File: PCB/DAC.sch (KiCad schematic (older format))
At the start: 3 parts, among them U9 DAC084S085C

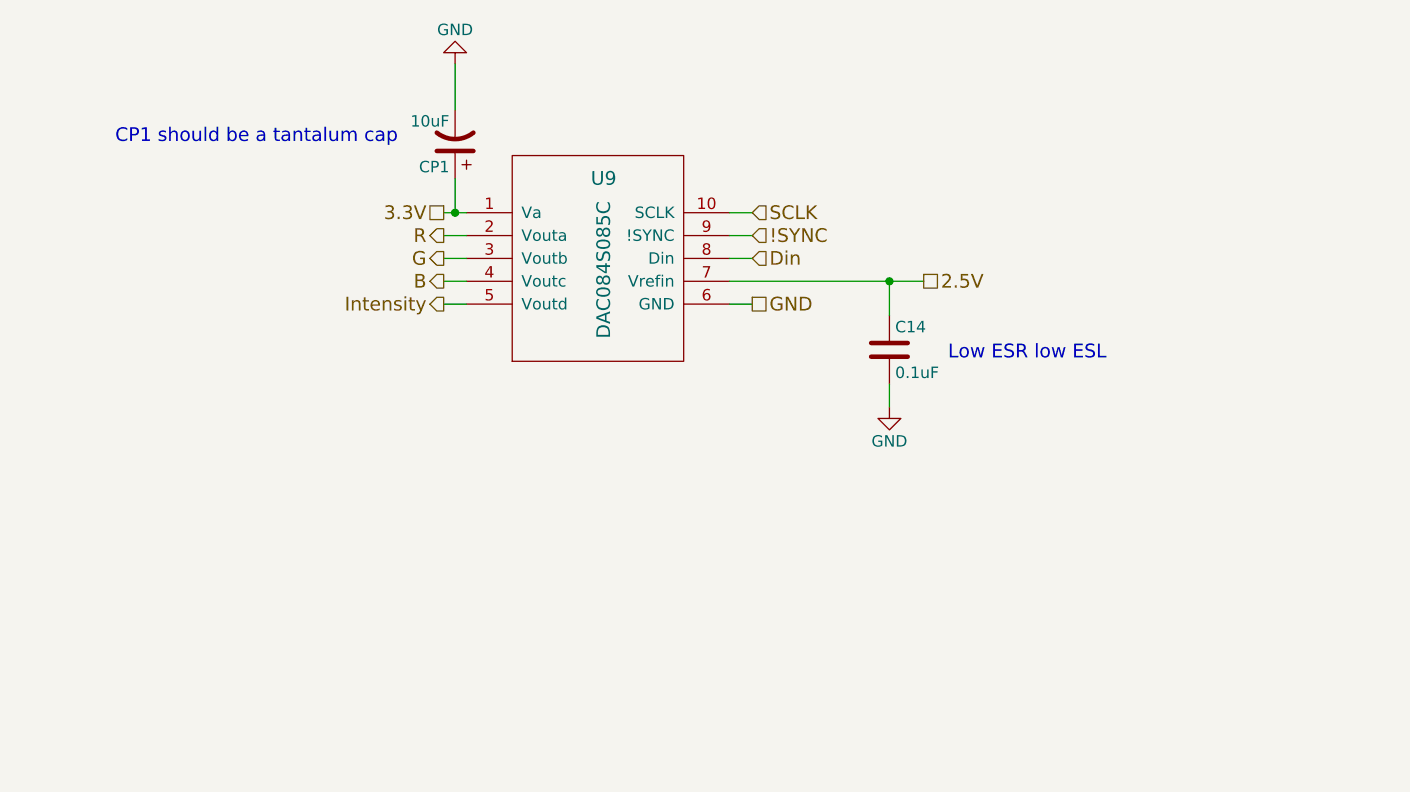
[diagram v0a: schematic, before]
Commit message: Generated BOM, fixed component names in schematic
Changed component names on output resistors and status LED to match that
in PCB
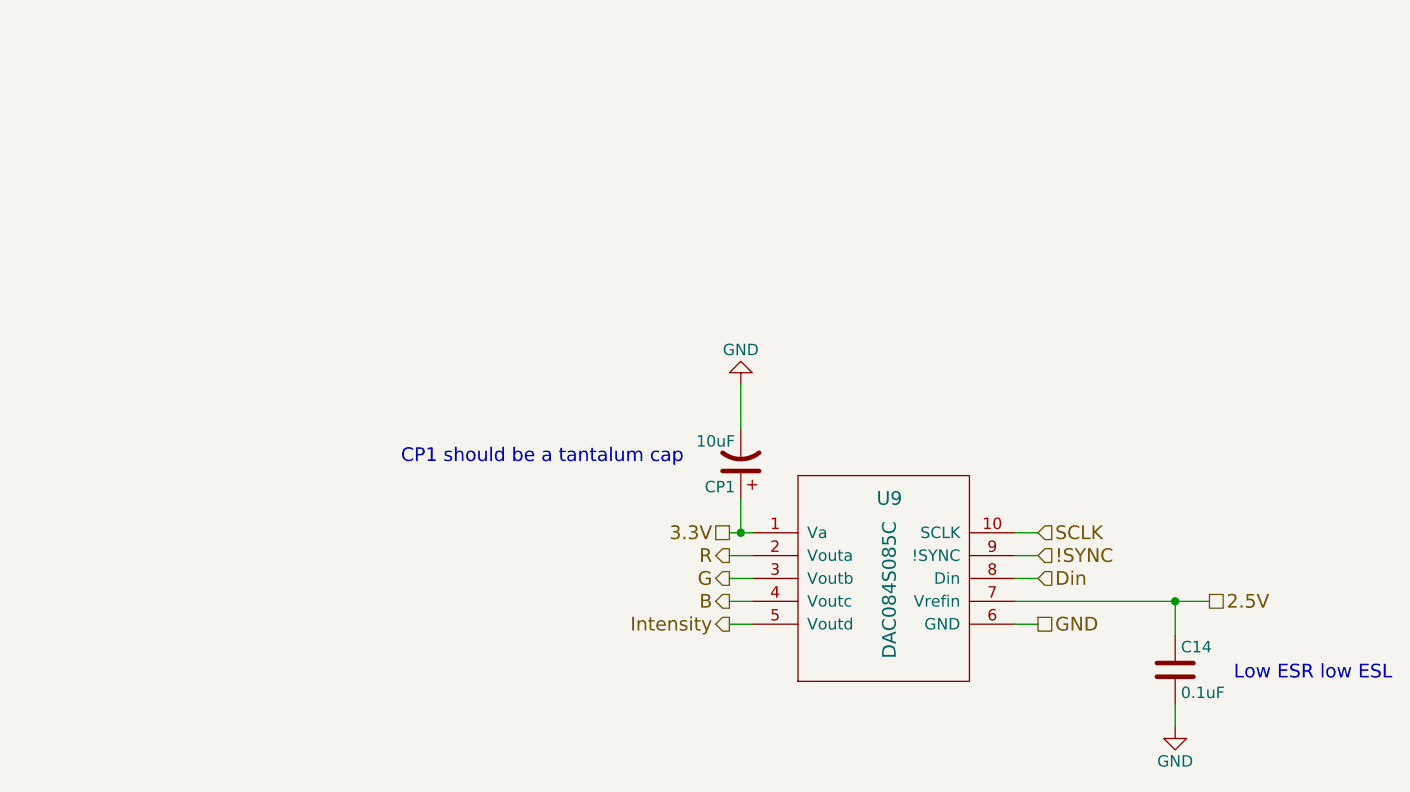
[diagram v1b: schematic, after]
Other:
- moved on the sheet: C14, CP1, U9
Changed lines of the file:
@@
 encoding utf-8
 Sheet 4 5
-Title ""
+Title "Digital to Analog Converter"
 Date ""
-Rev ""
+Rev "A"
 Comp ""
 Comment1 ""
@@
 L DAC084S085C U9
 U 1 1 56B20C0A
-P 4400 2650
-F 0 "U9" H 4400 3350 60  0000 C CNN
-F 1 "DAC084S085C" V 4400 2950 60  0000 C CNN
-F 2 "Housings_SSOP:MSOP-10_3x3mm_Pitch0.5mm" H 4400 2650 60  0001 C CNN
-F 3 "" H 4400 2650 60  0000 C CNN
-	1    4400 2650
+P 5650 4050
+F 0 "U9" H 5650 4750 60  0000 C CNN
+F 1 "DAC084S085C" V 5650 4350 60  0000 C CNN
+F 2 "Housings_SSOP:MSOP-10_3x3mm_Pitch0.5mm" H 5650 4050 60  0001 C CNN
+F 3 "" H 5650 4050 60  0000 C CNN
+	1    5650 4050
 	1    0    0    -1
 $EndComp
-Text HLabel 3700 2100 0    60   UnSpc ~ 0
+Text HLabel 4950 3500 0    60   UnSpc ~ 0
 3.3V
-Text HLabel 5050 2100 2    60   Input ~ 0
+Text HLabel 6300 3500 2    60   Input ~ 0
 SCLK
-Text HLabel 5050 2200 2    60   Input ~ 0
+Text HLabel 6300 3600 2    60   Input ~ 0
 !SYNC
-Text HLabel 5050 2300 2    60   Input ~ 0
+Text HLabel 6300 3700 2    60   Input ~ 0
 Din
-Text HLabel 5050 2500 2    60   UnSpc ~ 0
+Text HLabel 6300 3900 2    60   UnSpc ~ 0
 GND
-Text HLabel 3700 2200 0    60   Output ~ 0
+Text HLabel 4950 3600 0    60   Output ~ 0
 R
-Text HLabel 3700 2300 0    60   Output ~ 0
+Text HLabel 4950 3700 0    60   Output ~ 0
 G
-Text HLabel 3700 2400 0    60   Output ~ 0
+Text HLabel 4950 3800 0    60   Output ~ 0
 B
 $Comp
 L C C14
 U 1 1 56B32431
-P 5650 2700
-F 0 "C14" H 5675 2800 50  0000 L CNN
-F 1 "0.1uF" H 5675 2600 50  0000 L CNN
-F 2 "Capacitors_SMD:C_0402" H 5688 2550 50  0001 C CNN
-F 3 "" H 5650 2700 50  0000 C CNN
-	1    5650 2700
+P 6900 4100
+F 0 "C14" H 6925 4200 50  0000 L CNN
+F 1 "0.1uF" H 6925 4000 50  0000 L CNN
+F 2 "Capacitors_SMD:C_0402" H 6938 3950 50  0001 C CNN
+F 3 "" H 6900 4100 50  0000 C CNN
+	1    6900 4100
 	1    0    0    -1
 $EndComp
@@
 L GND #PWR025
 U 1 1 56B32486
-P 5650 2950
-F 0 "#PWR025" H 5650 2700 50  0001 C CNN
-F 1 "GND" H 5650 2800 50  0000 C CNN
-F 2 "" H 5650 2950 50  0000 C CNN
-F 3 "" H 5650 2950 50  0000 C CNN
-	1    5650 2950
+P 6900 4350
+F 0 "#PWR025" H 6900 4100 50  0001 C CNN
+F 1 "GND" H 6900 4200 50  0000 C CNN
+F 2 "" H 6900 4350 50  0000 C CNN
+F 3 "" H 6900 4350 50  0000 C CNN
+	1    6900 4350
 	1    0    0    -1
 $EndComp
-Text HLabel 5800 2400 2    60   UnSpc ~ 0
+Text HLabel 7050 3800 2    60   UnSpc ~ 0
 2.5V
 Wire Wire Line
-	3700 2100 3800 2100
+	4950 3500 5050 3500
 Wire Wire Line
-	3700 2200 3800 2200
+	4950 3600 5050 3600
 Wire Wire Line
-	3700 2300 3800 2300
+	4950 3700 5050 3700
 Wire Wire Line
-	3700 2400 3800 2400
+	4950 3800 5050 3800
 Wire Wire Line
-	4950 2100 5050 2100
+	6200 3500 6300 3500
 Wire Wire Line
-	4950 2200 5050 2200
+	6200 3600 6300 3600
 Wire Wire Line
-	4950 2300 5050 2300
+	6200 3700 6300 3700
 Wire Wire Line
-	4950 2500 5050 2500
+	6200 3900 6300 3900
 Wire Wire Line
-	4950 2400 5800 2400
+	6200 3800 7050 3800
 Wire Wire Line
-	5650 2400 5650 2550
+	6900 3800 6900 3950
 Wire Wire Line
-	5650 2950 5650 2850
-Connection ~ 5650 2400
+	6900 4350 6900 4250
+Connection ~ 6900 3800
 $Comp
 L CP1 CP1
 U 1 1 56B4306D
-P 3750 1800
-F 0 "CP1" H 3775 1900 50  0000 L CNN
-F 1 "10uF" H 3775 1700 50  0000 L CNN
-F 2 "Capacitors_Tantalum_SMD:TantalC_SizeA_EIA-3216_HandSoldering" H 3750 1800 50  0001 C CNN
-F 3 "" H 3750 1800 50  0000 C CNN
-	1    3750 1800
+P 5000 3200
+F 0 "CP1" H 5025 3300 50  0000 L CNN
+F 1 "10uF" H 5025 3100 50  0000 L CNN
+F 2 "Capacitors_Tantalum_SMD:TantalC_SizeA_EIA-3216_HandSoldering" H 5000 3200 50  0001 C CNN
+F 3 "" H 5000 3200 50  0000 C CNN
+	1    5000 3200
 	-1   0    0    1
 $EndComp
 Wire Wire Line
-	3750 1950 3750 2100
-Connection ~ 3750 2100
+	5000 3350 5000 3500
+Connection ~ 5000 3500
 $Comp
 L GND #PWR026
 U 1 1 56B430BD
-P 3750 1450
-F 0 "#PWR026" H 3750 1200 50  0001 C CNN
-F 1 "GND" H 3750 1300 50  0000 C CNN
-F 2 "" H 3750 1450 50  0000 C CNN
-F 3 "" H 3750 1450 50  0000 C CNN
-	1    3750 1450
+P 5000 2850
+F 0 "#PWR026" H 5000 2600 50  0001 C CNN
+F 1 "GND" H 5000 2700 50  0000 C CNN
+F 2 "" H 5000 2850 50  0000 C CNN
+F 3 "" H 5000 2850 50  0000 C CNN
+	1    5000 2850
 	-1   0    0    1
 $EndComp
 Wire Wire Line
-	3750 1450 3750 1650
-Text Notes 3500 1900 2    60   ~ 0
+	5000 2850 5000 3050
+Text Notes 4750 3300 2    60   ~ 0
 CP1 should be a tantalum cap\n\n
-Text Notes 6600 2750 2    60   ~ 0
+Text Notes 7850 4150 2    60   ~ 0
 Low ESR low ESL\n
-Text HLabel 3700 2500 0    60   Output ~ 0
+Text HLabel 4950 3900 0    60   Output ~ 0
 Intensity
 Wire Wire Line
-	3700 2500 3800 2500
+	4950 3900 5050 3900
 $EndSCHEMATC

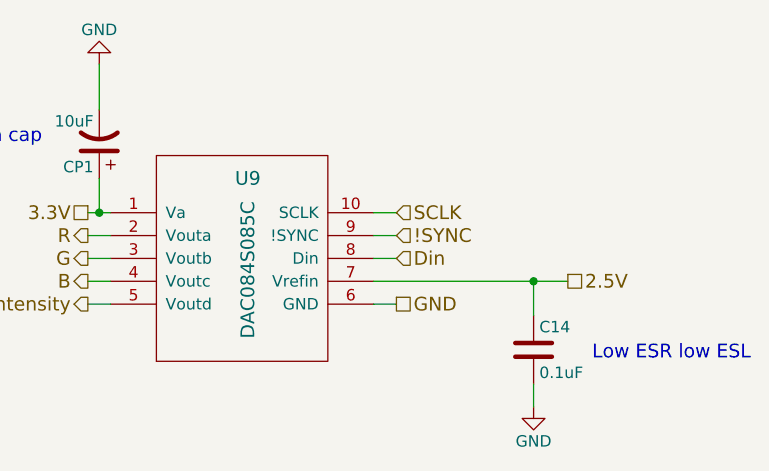
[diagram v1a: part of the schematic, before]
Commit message: Reannotated Components
Annotated components to standards,
TODO: Add Silkscreen for signals on bottom
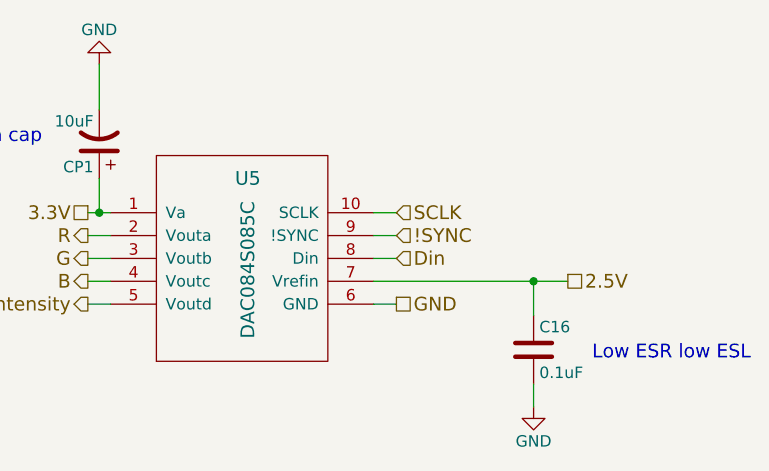
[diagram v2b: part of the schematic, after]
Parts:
- renumbered C14 to C16, U9 to U5
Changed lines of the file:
@@
 $EndDescr
 $Comp
-L DAC084S085C U9
+L DAC084S085C U5
 U 1 1 56B20C0A
 P 5650 4050
-F 0 "U9" H 5650 4750 60  0000 C CNN
+F 0 "U5" H 5650 4750 60  0000 C CNN
 F 1 "DAC084S085C" V 5650 4350 60  0000 C CNN
 F 2 "Housings_SSOP:MSOP-10_3x3mm_Pitch0.5mm" H 5650 4050 60  0001 C CNN
@@
 B
 $Comp
-L C C14
+L C C16
 U 1 1 56B32431
 P 6900 4100
-F 0 "C14" H 6925 4200 50  0000 L CNN
+F 0 "C16" H 6925 4200 50  0000 L CNN
 F 1 "0.1uF" H 6925 4000 50  0000 L CNN
 F 2 "Capacitors_SMD:C_0402" H 6938 3950 50  0001 C CNN

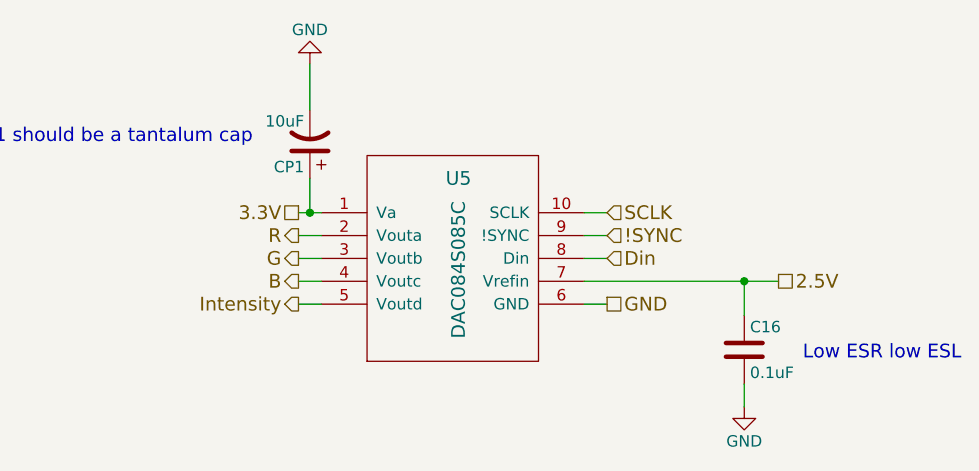
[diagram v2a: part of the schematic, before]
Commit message: Fixed schematic errors, "small" changes to PCB
Flipped DAC, changed component values, removed 1 capacitor, moved c16
from vref to power. Developed an urge to kill kicad
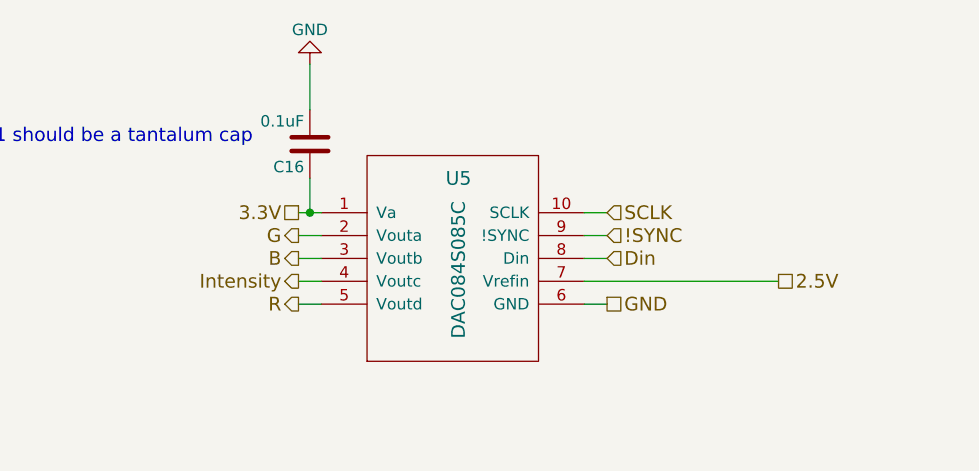
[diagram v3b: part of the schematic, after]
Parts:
- removed CP1: 10uF, Capacitors_Tantalum_SMD:TantalC_SizeA_EIA-3216_HandSoldering, symbol CP1
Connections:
- net 2.5V: no longer C16.1
- net 3.3V: now also C16.1
- net B: now also U5.3 (Voutb); no longer U5.4 (Voutc)
- net G: now also U5.2 (Vouta); no longer U5.3 (Voutb)
- net Intensity: now also U5.4 (Voutc); no longer U5.5 (Voutd)
- net R: now also U5.5 (Voutd); no longer U5.2 (Vouta)
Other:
- note removed: "Low ESR low ESL\n"
- moved on the sheet: C16
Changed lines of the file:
@@
 Text HLabel 6300 3900 2    60   UnSpc ~ 0
 GND
+Text HLabel 4950 3900 0    60   Output ~ 0
+R
 Text HLabel 4950 3600 0    60   Output ~ 0
-R
+G
 Text HLabel 4950 3700 0    60   Output ~ 0
-G
-Text HLabel 4950 3800 0    60   Output ~ 0
 B
 $Comp
 L C C16
 U 1 1 56B32431
-P 6900 4100
-F 0 "C16" H 6925 4200 50  0000 L CNN
-F 1 "0.1uF" H 6925 4000 50  0000 L CNN
-F 2 "Capacitors_SMD:C_0402" H 6938 3950 50  0001 C CNN
-F 3 "" H 6900 4100 50  0000 C CNN
-	1    6900 4100
-	1    0    0    -1
-$EndComp
-$Comp
-L GND #PWR025
-U 1 1 56B32486
-P 6900 4350
-F 0 "#PWR025" H 6900 4100 50  0001 C CNN
-F 1 "GND" H 6900 4200 50  0000 C CNN
-F 2 "" H 6900 4350 50  0000 C CNN
-F 3 "" H 6900 4350 50  0000 C CNN
-	1    6900 4350
-	1    0    0    -1
+P 5000 3200
+F 0 "C16" H 5025 3300 50  0000 L CNN
+F 1 "0.1uF" H 5025 3100 50  0000 L CNN
+F 2 "Capacitors_SMD:C_0402" H 5038 3050 50  0001 C CNN
+F 3 "" H 5000 3200 50  0000 C CNN
+	1    5000 3200
+	-1   0    0    1
 $EndComp
 Text HLabel 7050 3800 2    60   UnSpc ~ 0
@@
 	6200 3800 7050 3800
 Wire Wire Line
-	6900 3800 6900 3950
-Wire Wire Line
-	6900 4350 6900 4250
-Connection ~ 6900 3800
-$Comp
-L CP1 CP1
-U 1 1 56B4306D
-P 5000 3200
-F 0 "CP1" H 5025 3300 50  0000 L CNN
-F 1 "10uF" H 5025 3100 50  0000 L CNN
-F 2 "Capacitors_Tantalum_SMD:TantalC_SizeA_EIA-3216_HandSoldering" H 5000 3200 50  0001 C CNN
-F 3 "" H 5000 3200 50  0000 C CNN
-	1    5000 3200
-	-1   0    0    1
-$EndComp
-Wire Wire Line
 	5000 3350 5000 3500
 Connection ~ 5000 3500
 $Comp
-L GND #PWR026
+L GND #PWR025
 U 1 1 56B430BD
 P 5000 2850
-F 0 "#PWR026" H 5000 2600 50  0001 C CNN
+F 0 "#PWR025" H 5000 2600 50  0001 C CNN
 F 1 "GND" H 5000 2700 50  0000 C CNN
 F 2 "" H 5000 2850 50  0000 C CNN
@@
 Text Notes 4750 3300 2    60   ~ 0
 CP1 should be a tantalum cap\n\n
-Text Notes 7850 4150 2    60   ~ 0
-Low ESR low ESL\n
-Text HLabel 4950 3900 0    60   Output ~ 0
+Text HLabel 4950 3800 0    60   Output ~ 0
 Intensity
 Wire Wire Line
